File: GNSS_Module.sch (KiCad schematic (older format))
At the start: 10 parts

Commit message: Design Mic. Board
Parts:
- FB? (x2): MPN (none) -> BLM15HD102SN1
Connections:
- net GPS_Rx is gone; now on net GPS_RX: J?.5 (Pin_5)
- net GPS_Tx is gone; now on net GPS_TX: J?.4 (Pin_4)
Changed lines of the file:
@@
 $Descr A4 11693 8268
 encoding utf-8
-Sheet 2 13
+Sheet 2 14
 Title ""
 Date ""
@@
 F 2 "" V 3880 3900 50  0001 C CNN
 F 3 "~" H 3950 3900 50  0001 C CNN
+F 4 "BLM15HD102SN1" V 3950 3900 50  0001 C CNN "MPN"
 	1    3950 3900
 	0    1    1    0
@@
 	2650 3900 2750 3900
 Text Label 2550 2950 0    50   ~ 0
-GPS_Tx
+GPS_TX
 Text Label 2550 2850 0    50   ~ 0
-GPS_Rx
+GPS_RX
 Text Notes 2850 2950 0    50   ~ 0
 (GPS_LCD_TX_READY)
@@
 F 2 "" V 4030 3800 50  0001 C CNN
 F 3 "~" H 4100 3800 50  0001 C CNN
+F 4 "BLM15HD102SN1" V 4100 3800 50  0001 C CNN "MPN"
 	1    4100 3800
 	0    1    1    0

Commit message: Fix up some cap
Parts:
- CB?: value 1u -> 10u
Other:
- note added: "Doesn't require a small bypass \ncap (100nF). There is bypass \ncap on the GPS daughter board \nclose to the chip."
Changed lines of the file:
@@
 $Descr A4 11693 8268
 encoding utf-8
-Sheet 2 14
+Sheet 2 15
 Title ""
 Date ""
@@
 AR Path="/5EDF3693/5EE0528E" Ref="CB?"  Part="1"
 F 0 "CB?" H 1950 1600 50  0000 L CNN
-F 1 "1u" H 1900 1500 50  0000 L CNN
+F 1 "10u" H 1900 1500 50  0000 L CNN
 F 2 "" H 2100 1500 50  0001 C CNN
 F 3 "~" H 2100 1500 50  0001 C CNN
@@
 	1    0    0    -1
 $EndComp
+Text Notes 5000 1150 0    50   ~ 0
+Doesn't require a small bypass \ncap (100nF). There is bypass \ncap on the GPS daughter board \nclose to the chip.
 $EndSCHEMATC

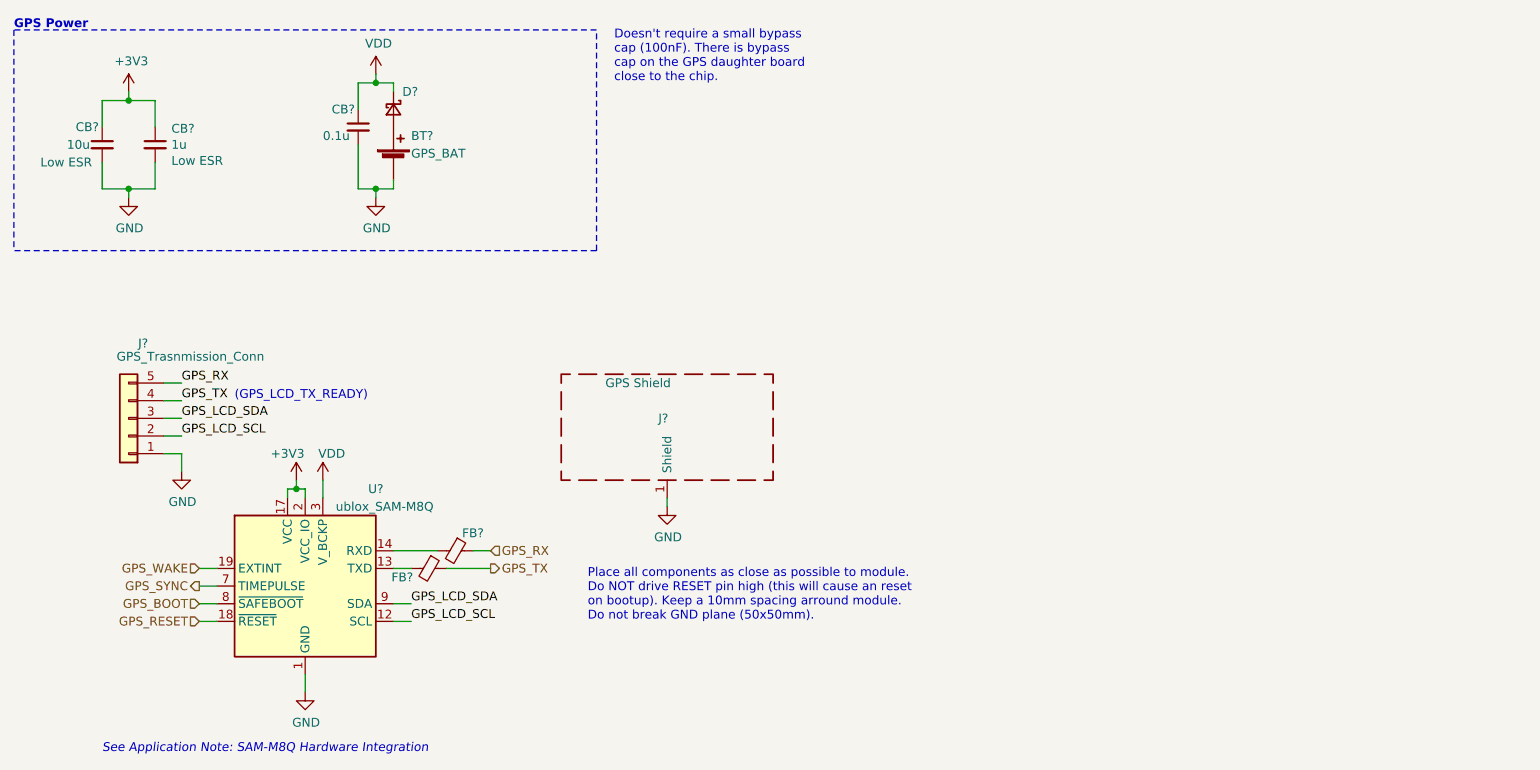
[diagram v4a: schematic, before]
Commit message: Design MCU section
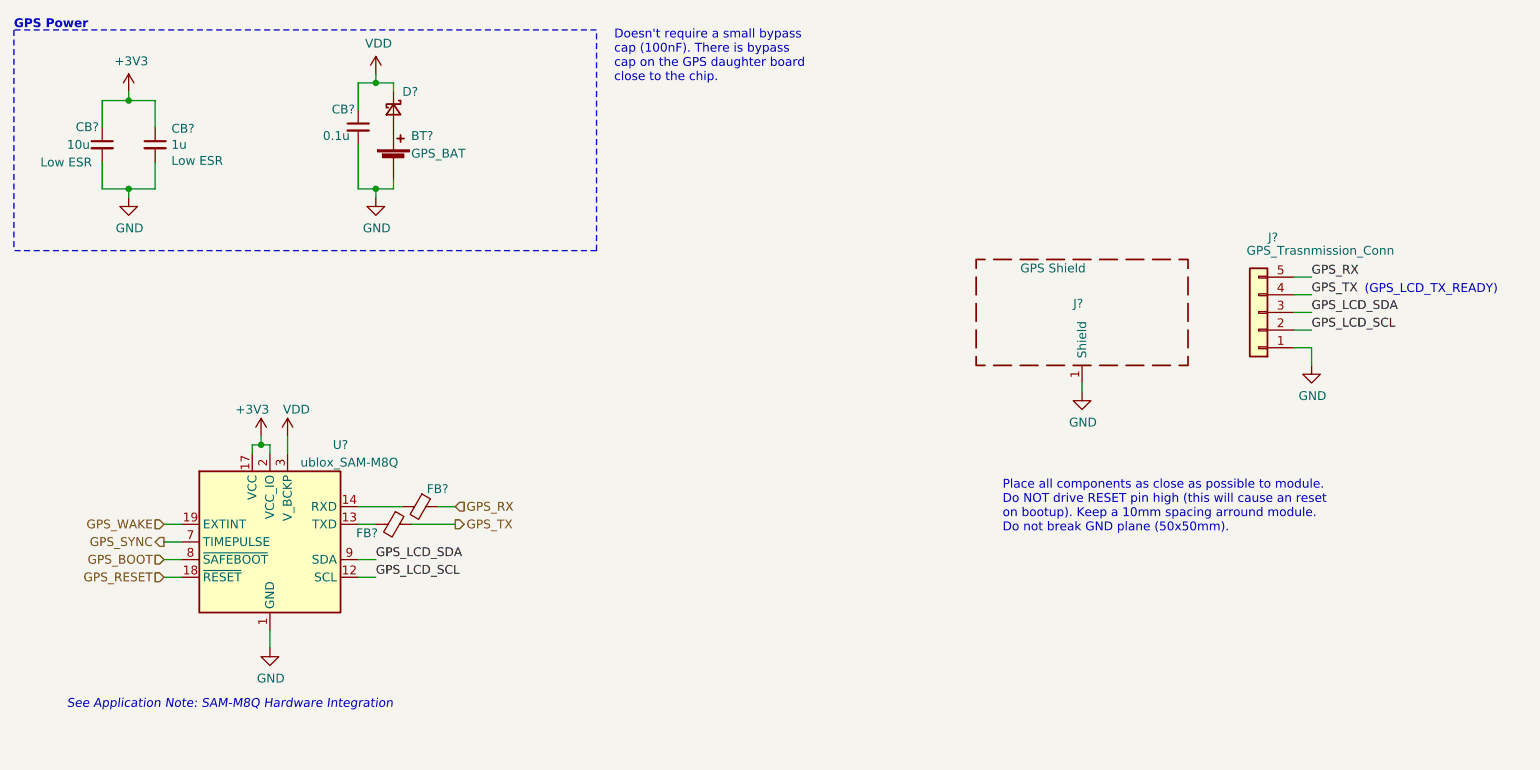
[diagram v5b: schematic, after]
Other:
- moved on the sheet: FB?, J?, U?
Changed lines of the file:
@@
 encoding utf-8
 Sheet 2 15
-Title ""
-Date ""
-Rev ""
-Comp ""
-Comment1 ""
-Comment2 ""
+Title "Kleinvoet"
+Date "2020-06-11"
+Rev "Rev. A"
+Comp "Department of Electronic Engineering - Stellenbosch University"
+Comment1 "Author: CM Geldenhuys <20198329@sun.ac.za>"
+Comment2 "Project: Kleinvoet"
 Comment3 ""
 Comment4 ""
@@
 L RF_GPS:ublox_SAM-M8Q U?
 U 1 1 5EE051F9
-P 3250 4000
+P 3050 3750
 AR Path="/5EE051F9" Ref="U?"  Part="1"
 AR Path="/5EDF3693/5EE051F9" Ref="U?"  Part="1"
-F 0 "U?" H 3650 4550 50  0000 C CNN
-F 1 "ublox_SAM-M8Q" H 3700 4450 50  0000 C CNN
-F 2 "RF_GPS:ublox_SAM-M8Q" H 3750 3550 50  0001 C CNN
-F 3 "https://www.u-blox.com/sites/default/files/SAM-M8Q_DataSheet_%28UBX-16012619%29.pdf" H 3250 4000 50  0001 C CNN
-	1    3250 4000
+F 0 "U?" H 3450 4300 50  0000 C CNN
+F 1 "ublox_SAM-M8Q" H 3500 4200 50  0000 C CNN
+F 2 "RF_GPS:ublox_SAM-M8Q" H 3550 3300 50  0001 C CNN
+F 3 "https://www.u-blox.com/sites/default/files/SAM-M8Q_DataSheet_%28UBX-16012619%29.pdf" H 3050 3750 50  0001 C CNN
+	1    3050 3750
 	1    0    0    -1
 $EndComp
@@
 L power:+3V3 #PWR?
 U 1 1 5EE05214
-P 3200 3400
+P 3000 3150
 AR Path="/5EE05214" Ref="#PWR?"  Part="1"
 AR Path="/5EDF3693/5EE05214" Ref="#PWR?"  Part="1"
-F 0 "#PWR?" H 3200 3250 50  0001 C CNN
-F 1 "+3V3" H 3150 3550 50  0000 C CNN
-F 2 "" H 3200 3400 50  0001 C CNN
-F 3 "" H 3200 3400 50  0001 C CNN
-	1    3200 3400
-	1    0    0    -1
-$EndComp
-Wire Wire Line
-	3200 3400 3200 3450
-Wire Wire Line
-	3200 3450 3250 3450
-Wire Wire Line
-	3250 3450 3250 3500
-Wire Wire Line
-	3200 3450 3150 3450
-Wire Wire Line
-	3150 3450 3150 3500
-Connection ~ 3200 3450
+F 0 "#PWR?" H 3000 3000 50  0001 C CNN
+F 1 "+3V3" H 2950 3300 50  0000 C CNN
+F 2 "" H 3000 3150 50  0001 C CNN
+F 3 "" H 3000 3150 50  0001 C CNN
+	1    3000 3150
+	1    0    0    -1
+$EndComp
+Wire Wire Line
+	3000 3150 3000 3200
+Wire Wire Line
+	3000 3200 3050 3200
+Wire Wire Line
+	3050 3200 3050 3250
+Wire Wire Line
+	3000 3200 2950 3200
+Wire Wire Line
+	2950 3200 2950 3250
+Connection ~ 3000 3200
 Wire Wire Line
 	2100 1250 2250 1250
@@
 Text Notes 1600 850  0    50   ~ 10
 GPS Power
-Text Label 3850 4100 0    50   ~ 0
+Text Label 3650 3850 0    50   ~ 0
 GPS_LCD_SDA
-Text Label 3850 4200 0    50   ~ 0
+Text Label 3650 3950 0    50   ~ 0
 GPS_LCD_SCL
 Wire Wire Line
-	2650 4200 2750 4200
-Wire Wire Line
-	2650 4100 2750 4100
+	2450 3950 2550 3950
+Wire Wire Line
+	2450 3850 2550 3850
 Wire Notes Line
 	4900 2100 1600 2100
@@
 L power:GND #PWR?
 U 1 1 5EE05234
-P 3250 4600
+P 3050 4350
 AR Path="/5EE05234" Ref="#PWR?"  Part="1"
 AR Path="/5EDF3693/5EE05234" Ref="#PWR?"  Part="1"
-F 0 "#PWR?" H 3250 4350 50  0001 C CNN
-F 1 "GND" H 3255 4427 50  0000 C CNN
-F 2 "" H 3250 4600 50  0001 C CNN
-F 3 "" H 3250 4600 50  0001 C CNN
-	1    3250 4600
-	1    0    0    -1
-$EndComp
-Wire Wire Line
-	3250 4500 3250 4600
+F 0 "#PWR?" H 3050 4100 50  0001 C CNN
+F 1 "GND" H 3055 4177 50  0000 C CNN
+F 2 "" H 3050 4350 50  0001 C CNN
+F 3 "" H 3050 4350 50  0001 C CNN
+	1    3050 4350
+	1    0    0    -1
+$EndComp
+Wire Wire Line
+	3050 4250 3050 4350
 $Comp
 L Device:Ferrite_Bead_Small FB?
 U 1 1 5EE05241
-P 3950 3900
+P 3750 3650
 AR Path="/5EE05241" Ref="FB?"  Part="1"
 AR Path="/5EDF3693/5EE05241" Ref="FB?"  Part="1"
-F 0 "FB?" V 4000 3750 50  0000 C CNN
-F 1 "BLM15HD102SN1" V 4000 4250 50  0001 C CNN
-F 2 "" V 3880 3900 50  0001 C CNN
-F 3 "~" H 3950 3900 50  0001 C CNN
-F 4 "BLM15HD102SN1" V 3950 3900 50  0001 C CNN "MPN"
-	1    3950 3900
+F 0 "FB?" V 3800 3500 50  0000 C CNN
+F 1 "BLM15HD102SN1" V 3800 4000 50  0001 C CNN
+F 2 "" V 3680 3650 50  0001 C CNN
+F 3 "~" H 3750 3650 50  0001 C CNN
+F 4 "BLM15HD102SN1" V 3750 3650 50  0001 C CNN "MPN"
+	1    3750 3650
 	0    1    1    0
 $EndComp
 Wire Wire Line
-	3750 4100 3850 4100
-Wire Wire Line
-	3750 4200 3850 4200
+	3550 3850 3650 3850
+Wire Wire Line
+	3550 3950 3650 3950
 $Comp
 L Connector_Generic:Conn_01x05 J?
 U 1 1 5EE05249
-P 2250 3050
+P 8650 2450
 AR Path="/5EE05249" Ref="J?"  Part="1"
 AR Path="/5EDF3693/5EE05249" Ref="J?"  Part="1"
-F 0 "J?" H 2168 2625 50  0000 C CNN
-F 1 "GPS_Trasnmission_Conn" H 1900 2700 50  0000 C CNN
-F 2 "" H 2250 3050 50  0001 C CNN
-F 3 "~" H 2250 3050 50  0001 C CNN
-	1    2250 3050
+F 0 "J?" H 8568 2025 50  0000 C CNN
+F 1 "GPS_Trasnmission_Conn" H 8300 2100 50  0000 C CNN
+F 2 "" H 8650 2450 50  0001 C CNN
+F 3 "~" H 8650 2450 50  0001 C CNN
+	1    8650 2450
 	-1   0    0    1
 $EndComp
@@
 L power:GND #PWR?
 U 1 1 5EE0524F
-P 2550 3350
+P 8950 2750
 AR Path="/5EE0524F" Ref="#PWR?"  Part="1"
 AR Path="/5EDF3693/5EE0524F" Ref="#PWR?"  Part="1"
-F 0 "#PWR?" H 2550 3100 50  0001 C CNN
-F 1 "GND" H 2555 3177 50  0000 C CNN
-F 2 "" H 2550 3350 50  0001 C CNN
-F 3 "" H 2550 3350 50  0001 C CNN
-	1    2550 3350
-	1    0    0    -1
-$EndComp
-Wire Wire Line
-	2550 3350 2550 3250
-Wire Wire Line
-	2550 3250 2450 3250
-Text Label 2550 3150 0    50   ~ 0
+F 0 "#PWR?" H 8950 2500 50  0001 C CNN
+F 1 "GND" H 8955 2577 50  0000 C CNN
+F 2 "" H 8950 2750 50  0001 C CNN
+F 3 "" H 8950 2750 50  0001 C CNN
+	1    8950 2750
+	1    0    0    -1
+$EndComp
+Wire Wire Line
+	8950 2750 8950 2650
+Wire Wire Line
+	8950 2650 8850 2650
+Text Label 8950 2550 0    50   ~ 0
 GPS_LCD_SCL
-Text Label 2550 3050 0    50   ~ 0
+Text Label 8950 2450 0    50   ~ 0
 GPS_LCD_SDA
 Wire Wire Line
-	2650 3900 2750 3900
-Text Label 2550 2950 0    50   ~ 0
+	2450 3650 2550 3650
+Text Label 8950 2350 0    50   ~ 0
 GPS_TX
-Text Label 2550 2850 0    50   ~ 0
+Text Label 8950 2250 0    50   ~ 0
 GPS_RX
-Text Notes 2850 2950 0    50   ~ 0
+Text Notes 9250 2350 0    50   ~ 0
 (GPS_LCD_TX_READY)
 Wire Wire Line
-	2550 2850 2450 2850
-Wire Wire Line
-	2550 2950 2450 2950
-Wire Wire Line
-	2550 3050 2450 3050
-Wire Wire Line
-	2550 3150 2450 3150
-Wire Wire Line
-	3750 3900 3850 3900
-Text Notes 2100 4950 0    50   Italic 0
+	8950 2250 8850 2250
+Wire Wire Line
+	8950 2350 8850 2350
+Wire Wire Line
+	8950 2450 8850 2450
+Wire Wire Line
+	8950 2550 8850 2550
+Wire Wire Line
+	3550 3650 3650 3650
+Text Notes 1900 4700 0    50   Italic 0
 See Application Note: SAM-M8Q Hardware Integration
-Text Notes 4850 4200 0    50   ~ 0
+Text Notes 7200 3700 0    50   ~ 0
 Place all components as close as possible to module. \nDo NOT drive RESET pin high (this will cause an reset \non bootup). Keep a 10mm spacing arround module. \nDo not break GND plane (50x50mm).
 $Comp
@@
 	3750 1150 3750 1200
 Wire Wire Line
-	2650 4000 2750 4000
+	2450 3750 2550 3750
 $Comp
 L power:GND #PWR?
 U 1 1 5EE052A0
-P 5300 3550
+P 7650 2900
 AR Path="/5EE052A0" Ref="#PWR?"  Part="1"
 AR Path="/5EDF3693/5EE052A0" Ref="#PWR?"  Part="1"
-F 0 "#PWR?" H 5300 3300 50  0001 C CNN
-F 1 "GND" H 5305 3377 50  0000 C CNN
-F 2 "" H 5300 3550 50  0001 C CNN
-F 3 "" H 5300 3550 50  0001 C CNN
-	1    5300 3550
-	1    0    0    -1
-$EndComp
-Wire Wire Line
-	5300 3550 5300 3500
+F 0 "#PWR?" H 7650 2650 50  0001 C CNN
+F 1 "GND" H 7655 2727 50  0000 C CNN
+F 2 "" H 7650 2900 50  0001 C CNN
+F 3 "" H 7650 2900 50  0001 C CNN
+	1    7650 2900
+	1    0    0    -1
+$EndComp
+Wire Wire Line
+	7650 2900 7650 2850
 $Comp
 L power:VDD #PWR?
@@
 L power:VDD #PWR?
 U 1 1 5EE052B2
-P 3350 3400
+P 3150 3150
 AR Path="/5EE052B2" Ref="#PWR?"  Part="1"
 AR Path="/5EDF3693/5EE052B2" Ref="#PWR?"  Part="1"
-F 0 "#PWR?" H 3350 3250 50  0001 C CNN
-F 1 "VDD" H 3400 3550 50  0000 C CNN
-F 2 "" H 3350 3400 50  0001 C CNN
-F 3 "" H 3350 3400 50  0001 C CNN
-	1    3350 3400
-	1    0    0    -1
-$EndComp
-Wire Wire Line
-	3350 3400 3350 3500
-Text HLabel 4300 3800 2    50   Input ~ 0
+F 0 "#PWR?" H 3150 3000 50  0001 C CNN
+F 1 "VDD" H 3200 3300 50  0000 C CNN
+F 2 "" H 3150 3150 50  0001 C CNN
+F 3 "" H 3150 3150 50  0001 C CNN
+	1    3150 3150
+	1    0    0    -1
+$EndComp
+Wire Wire Line
+	3150 3150 3150 3250
+Text HLabel 4100 3550 2    50   Input ~ 0
 GPS_RX
 $Comp
 L Device:Ferrite_Bead_Small FB?
 U 1 1 5EE19301
-P 4100 3800
+P 3900 3550
 AR Path="/5EE19301" Ref="FB?"  Part="1"
 AR Path="/5EDF3693/5EE19301" Ref="FB?"  Part="1"
-F 0 "FB?" V 4000 3900 50  0000 C CNN
-F 1 "BLM15HD102SN1" V 4150 4150 50  0001 C CNN
-F 2 "" V 4030 3800 50  0001 C CNN
-F 3 "~" H 4100 3800 50  0001 C CNN
-F 4 "BLM15HD102SN1" V 4100 3800 50  0001 C CNN "MPN"
-	1    4100 3800
+F 0 "FB?" V 3800 3650 50  0000 C CNN
+F 1 "BLM15HD102SN1" V 3950 3900 50  0001 C CNN
+F 2 "" V 3830 3550 50  0001 C CNN
+F 3 "~" H 3900 3550 50  0001 C CNN
+F 4 "BLM15HD102SN1" V 3900 3550 50  0001 C CNN "MPN"
+	1    3900 3550
 	0    1    1    0
 $EndComp
 Wire Wire Line
-	3750 3800 4000 3800
-Wire Wire Line
-	4300 3800 4200 3800
-Text HLabel 4300 3900 2    50   Output ~ 0
+	3550 3550 3800 3550
+Wire Wire Line
+	4100 3550 4000 3550
+Text HLabel 4100 3650 2    50   Output ~ 0
 GPS_TX
 Wire Wire Line
-	4050 3900 4300 3900
-Text HLabel 2650 3900 0    50   Input ~ 0
+	3850 3650 4100 3650
+Text HLabel 2450 3650 0    50   Input ~ 0
 GPS_WAKE
-Text HLabel 2650 4000 0    50   Output ~ 0
+Text HLabel 2450 3750 0    50   Output ~ 0
 GPS_SYNC
-Text HLabel 2650 4100 0    50   Input ~ 0
+Text HLabel 2450 3850 0    50   Input ~ 0
 GPS_BOOT
-Text HLabel 2650 4200 0    50   Input ~ 0
+Text HLabel 2450 3950 0    50   Input ~ 0
 GPS_RESET
 $Comp
 L Device:RF_Shield_One_Piece J?
 U 1 1 5EE0529A
-P 5300 3100
+P 7650 2450
 AR Path="/5EE0529A" Ref="J?"  Part="1"
 AR Path="/5EDF3693/5EE0529A" Ref="J?"  Part="1"
-F 0 "J?" H 5250 3150 50  0000 L CNN
-F 1 "GPS Shield" H 4950 3350 50  0000 L CNN
-F 2 "" H 5300 3000 50  0001 C CNN
-F 3 "~" H 5300 3000 50  0001 C CNN
-	1    5300 3100
-	1    0    0    -1
-$EndComp
+F 0 "J?" H 7600 2500 50  0000 L CNN
+F 1 "GPS Shield" H 7300 2700 50  0000 L CNN
+F 2 "" H 7650 2350 50  0001 C CNN
+F 3 "~" H 7650 2350 50  0001 C CNN
+	1    7650 2450
+	1    0    0    -1
+$EndComp

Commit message: Finalise design
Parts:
- added TP? (x2): TestPoint, symbol Connector:TestPoint
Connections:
- net GPS_RX: now also FB?.1, TP?.1; no longer FB?.1
- net GPS_TX: now also FB?.1, TP?.1; no longer FB?.1
- net GPS_BOOT renamed GPS_~SAFEBOOT
- net GPS_RESET renamed GPS_~RESET
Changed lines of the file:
@@
 $Descr A4 11693 8268
 encoding utf-8
-Sheet 2 15
+Sheet 15 15
 Title "Kleinvoet"
 Date "2020-06-11"
@@
 Wire Wire Line
 	3150 3150 3150 3250
-Text HLabel 4100 3550 2    50   Input ~ 0
+Text HLabel 4300 3650 2    50   Output ~ 0
 GPS_RX
 $Comp
@@
 Wire Wire Line
 	3550 3550 3800 3550
-Wire Wire Line
-	4100 3550 4000 3550
-Text HLabel 4100 3650 2    50   Output ~ 0
+Text HLabel 4300 3550 2    50   Input ~ 0
 GPS_TX
 Wire Wire Line
-	3850 3650 4100 3650
+	3850 3650 4200 3650
 Text HLabel 2450 3650 0    50   Input ~ 0
 GPS_WAKE
@@
 GPS_SYNC
 Text HLabel 2450 3850 0    50   Input ~ 0
-GPS_BOOT
+GPS_~SAFEBOOT
 Text HLabel 2450 3950 0    50   Input ~ 0
-GPS_RESET
+GPS_~RESET
 $Comp
 L Device:RF_Shield_One_Piece J?
@@
 Text Notes 5000 1150 0    50   ~ 0
 Doesn't require a small bypass \ncap (100nF). There is bypass \ncap on the GPS daughter board \nclose to the chip.
+$Comp
+L Connector:TestPoint TP?
+U 1 1 5F029AD8
+P 4200 3650
+F 0 "TP?" H 4142 3722 50  0000 R CNN
+F 1 "TestPoint" H 4258 3677 50  0001 L CNN
+F 2 "" H 4400 3650 50  0001 C CNN
+F 3 "~" H 4400 3650 50  0001 C CNN
+	1    4200 3650
+	-1   0    0    1
+$EndComp
+Connection ~ 4200 3650
+Wire Wire Line
+	4200 3650 4300 3650
+$Comp
+L Connector:TestPoint TP?
+U 1 1 5F029627
+P 4200 3550
+F 0 "TP?" H 4258 3622 50  0000 L CNN
+F 1 "TestPoint" H 4258 3577 50  0001 L CNN
+F 2 "" H 4400 3550 50  0001 C CNN
+F 3 "~" H 4400 3550 50  0001 C CNN
+	1    4200 3550
+	1    0    0    -1
+$EndComp
+Wire Wire Line
+	4000 3550 4200 3550
+Connection ~ 4200 3550
+Wire Wire Line
+	4200 3550 4300 3550
 $EndSCHEMATC
